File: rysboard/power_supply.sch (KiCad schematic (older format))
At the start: 34 parts, among them J19 Fan_Connector, Q4 DMP3036SSD-13, Q5 DMP3036SSD-13, U3 ST1S10, U6 L78L33_SO8

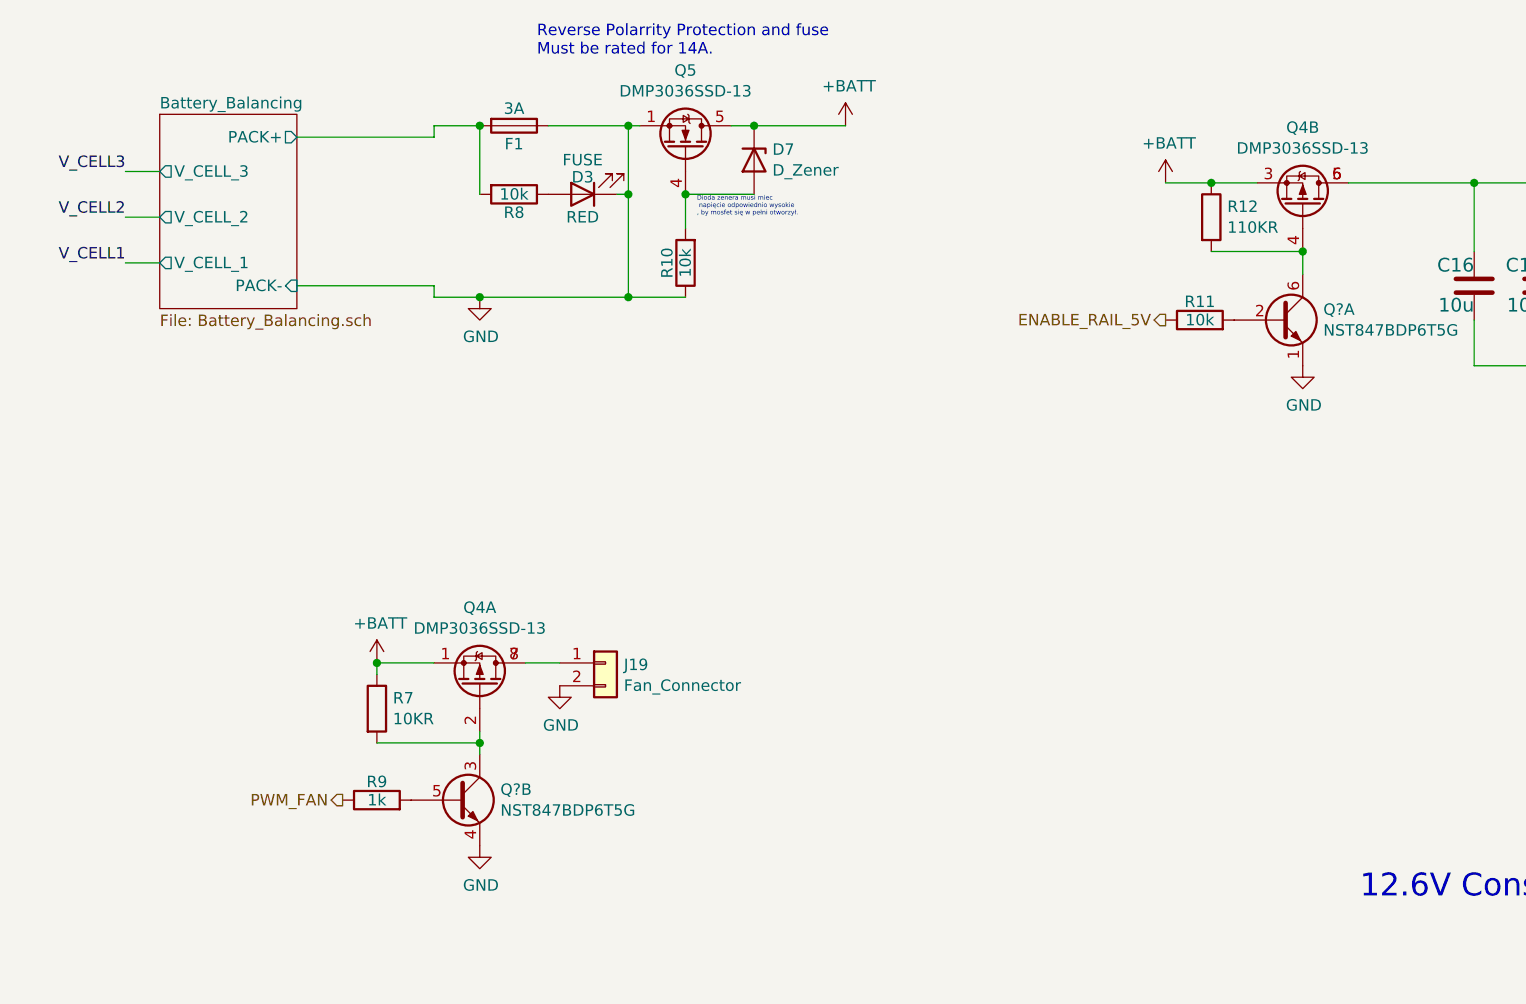
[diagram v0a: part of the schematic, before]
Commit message: added some of the analog sensors
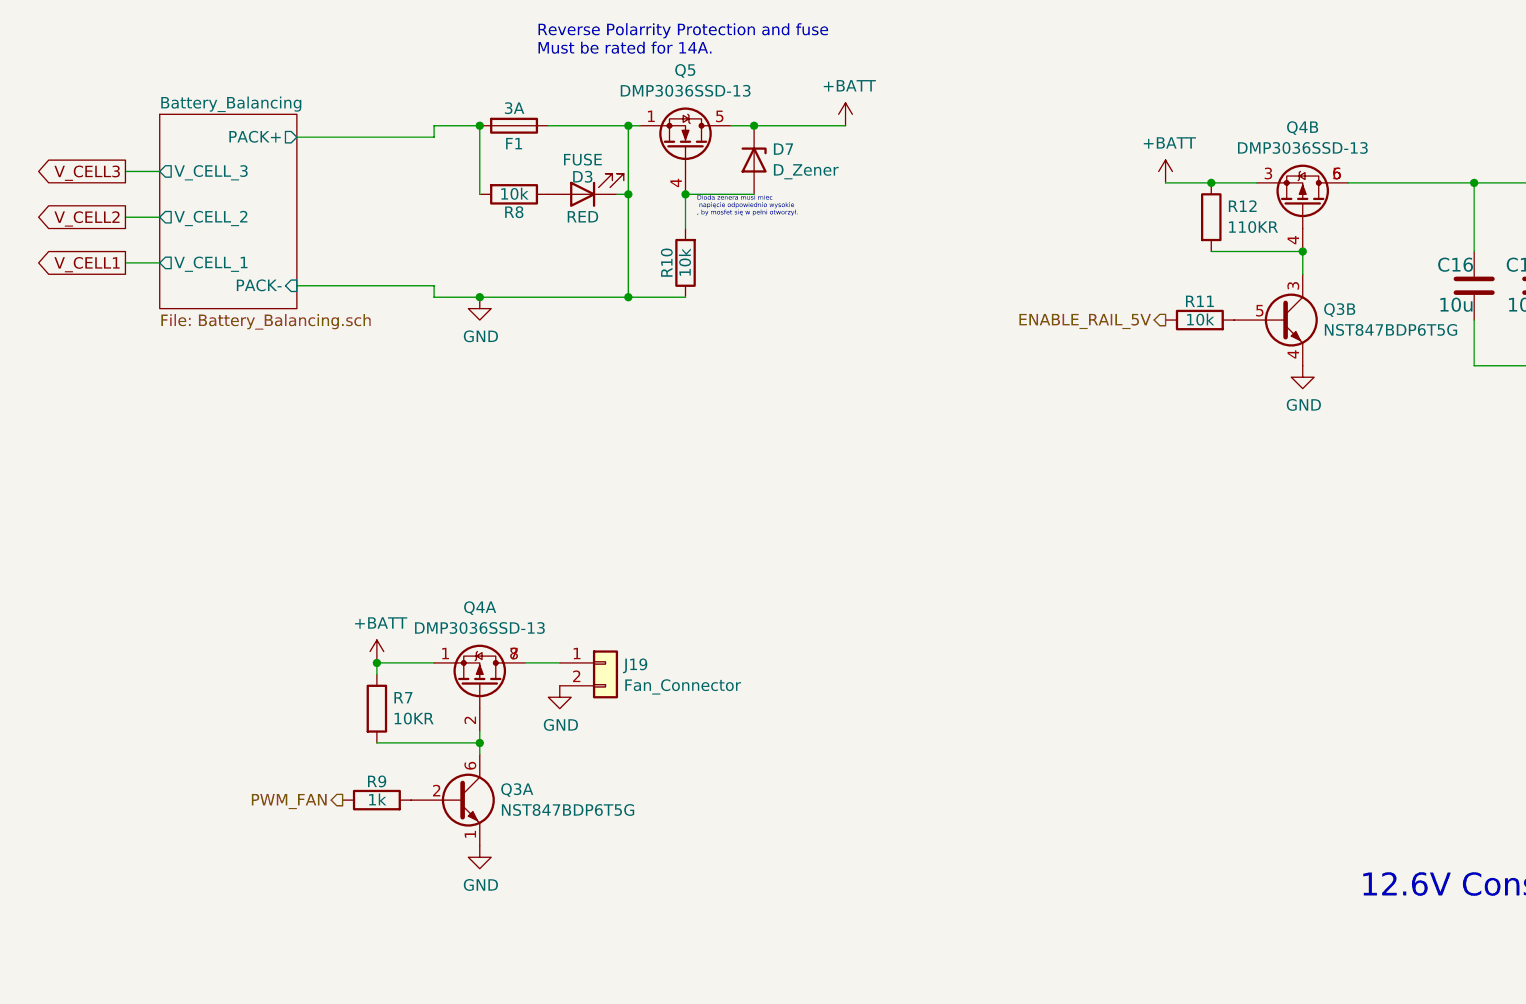
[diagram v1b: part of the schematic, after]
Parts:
- gave numbers to parts that had none: 1
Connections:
- net GND: now also Q3.1 (E1), Q3.4 (E2); no longer Q3.1 (E1), Q3.4 (E2)
- net at Q4.4 (G2), R12.2: now also Q3.3 (C2); no longer Q3.6 (C1)
- net at R11.2: now also Q3.5 (B2); no longer Q3.2 (B1)
- net at R9.2: now also Q3.2 (B1); no longer Q3.5 (B2)
- net at Q4.2 (G1), R7.2: now also Q3.6 (C1); no longer Q3.3 (C2)
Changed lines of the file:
@@
 Wire Wire Line
 	1000 1500 850  1500
-Text Label 850  1300 2    50   ~ 0
-V_CELL3
-Text Label 850  1500 2    50   ~ 0
-V_CELL2
-Text Label 850  1700 2    50   ~ 0
-V_CELL1
 $Sheet
 S 1000 1050 600  850
@@
 	7800 5300 7650 5300
 $Comp
-L rysboard:NST847BDP6T5G Q?
-U 1 1 606E7E9A
+L rysboard:NST847BDP6T5G Q3
+U 2 1 606E7E9A
 P 5900 1950
-F 0 "Q?" H 6090 1996 50  0000 L CNN
+F 0 "Q3" H 6090 1996 50  0000 L CNN
 F 1 "NST847BDP6T5G" H 6090 1905 50  0000 L CNN
 F 2 "Package_TO_SOT_SMD:SOT-963" H 6100 2050 50  0001 C CNN
 F 3 "~" H 5900 1950 50  0001 C CNN
-	1    5900 1950
-	1    0    0    -1
-$EndComp
-$Comp
-L rysboard:NST847BDP6T5G Q?
-U 2 1 606E8E92
+	2    5900 1950
+	1    0    0    -1
+$EndComp
+$Comp
+L rysboard:NST847BDP6T5G Q3
+U 1 1 606E8E92
 P 2300 4050
-F 0 "Q?" H 2490 4096 50  0000 L CNN
+F 0 "Q3" H 2490 4096 50  0000 L CNN
 F 1 "NST847BDP6T5G" H 2490 4005 50  0000 L CNN
 F 2 "Package_TO_SOT_SMD:SOT-963" H 2500 4150 50  0001 C CNN
 F 3 "~" H 2300 4050 50  0001 C CNN
-	2    2300 4050
-	1    0    0    -1
-$EndComp
+	1    2300 4050
+	1    0    0    -1
+$EndComp
+Text GLabel 850  1300 0    50   Output ~ 0
+V_CELL3
+Text GLabel 850  1500 0    50   Output ~ 0
+V_CELL2
+Text GLabel 850  1700 0    50   Output ~ 0
+V_CELL1
 $EndSCHEMATC

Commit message: Added eval board for STM32G031K8U6, rybsoard layout done, exact vals yet to be calculated
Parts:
- J19: symbol Connector_Generic:Conn_01x02 -> Connector_Generic:Conn_01x03
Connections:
- net GND: now also J19.3 (Pin_3); no longer J19.2 (Pin_2)
- net at Q4.7 (d), Q4.8 (d): now also J19.2 (Pin_2); no longer J19.1 (Pin_1)
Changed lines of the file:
@@
 Connection ~ 1950 3450
 $Comp
-L Connector_Generic:Conn_01x02 J19
+L Connector_Generic:Conn_01x03 J19
 U 1 1 606189C6
 P 2950 3450

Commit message: sensors enable added, Vref problem to solve
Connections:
- net GND: no longer F1.1, Q5.1 (S), Q5.2 (S), Q5.3 (S)
- new net: F1.1, Q5.1 (S), Q5.2 (S), Q5.3 (S)
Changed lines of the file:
@@
 $EndComp
-Wire Wire Line
-	3050 1100 2700 1100
-Connection ~ 3050 1100
 Wire Wire Line
 	2400 1100 2400 1400
 Wire Wire Line
 	3000 1400 3050 1400
-Wire Wire Line
-	3050 1400 3050 1100
 $Comp
 L power:GND #PWR018
@@
 	-1   0    0    1
 $EndComp
-Wire Wire Line
-	3100 1100 3050 1100
 $Comp
 L Device:R R8
@@
 Wire Wire Line
 	3050 1400 3050 1850
-Connection ~ 3050 1400
 Connection ~ 3050 1850
 Wire Wire Line
@@
 Text GLabel 850  1700 0    50   Output ~ 0
 V_CELL1
+Wire Wire Line
+	2700 1100 3100 1100
 $EndSCHEMATC

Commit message: new mosfet footprints
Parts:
- R12, R7: footprint (none) -> Resistor_SMD:R_0603_1608Metric
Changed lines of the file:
@@
 F 0 "R12" H 5670 1546 50  0000 L CNN
 F 1 "110KR" H 5670 1455 50  0000 L CNN
-F 2 "" V 5530 1500 50  0001 C CNN
+F 2 "Resistor_SMD:R_0603_1608Metric" V 5530 1500 50  0001 C CNN
 F 3 "~" H 5600 1500 50  0001 C CNN
 	1    5600 1500
@@
 F 0 "R7" H 2020 3696 50  0000 L CNN
 F 1 "10KR" H 2020 3605 50  0000 L CNN
-F 2 "" V 1880 3650 50  0001 C CNN
+F 2 "Resistor_SMD:R_0603_1608Metric" V 1880 3650 50  0001 C CNN
 F 3 "~" H 1950 3650 50  0001 C CNN
 	1    1950 3650

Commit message: Fixed library, added a few MOSFET layouts
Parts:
- removed D4, D5, D6: SK52, Diode_SMD:D_SMB, symbol Device:D_Schottky
- removed unit 1 of Q4
- removed Q5: DMP3036SSD-13, Package_SO:SO-8_5.3x6.2mm_P1.27mm, symbol Transistor_FET:Si7450DP
- added Q5: DMP3036SSD-13, Package_SO:SO-8_3.9x4.9mm_P1.27mm, symbol rysboard:DMP3036SSD-13
- added Q?: DMP2075UFDB, SamacSys_Parts:DMP2075UFDB7, symbol rysboard:DMP2075UFDB
- Q4: footprint Package_SO:SO-8_5.3x6.2mm_P1.27mm -> Package_SO:SO-8_3.9x4.9mm_P1.27mm
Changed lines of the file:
@@
 F 1 "1uF" H 2550 6950 60  0000 R TNN
 F 2 "Capacitor_SMD:C_0603_1608Metric" H 2450 7090 60  0001 C CNN
-F 3 "" H 2450 7090 60  0001 C CNN
+F 3 "~" H 2450 7090 60  0001 C CNN
 	1    2550 7000
 	1    0    0    -1
@@
 F 1 "100n" H 3750 6950 60  0000 R TNN
 F 2 "Capacitor_SMD:C_0603_1608Metric" H 3650 7090 60  0001 C CNN
-F 3 "" H 3650 7090 60  0001 C CNN
+F 3 "~" H 3650 7090 60  0001 C CNN
 	1    3750 7000
 	1    0    0    -1
@@
 F 1 "10u" H 9875 1750 60  0000 R TNN
 F 2 "Capacitor_SMD:C_1206_3216Metric" H 9775 1890 60  0001 C CNN
-F 3 "" H 9775 1890 60  0000 C CNN
+F 3 "~" H 9775 1890 60  0000 C CNN
 	1    9875 1800
 	1    0    0    -1
@@
 F 1 "10u" H 10175 1750 60  0000 R TNN
 F 2 "Capacitor_SMD:C_1206_3216Metric" H 10075 1890 60  0001 C CNN
-F 3 "" H 10075 1890 60  0000 C CNN
+F 3 "~" H 10075 1890 60  0000 C CNN
 	1    10175 1800
 	1    0    0    -1
@@
 F 1 "100n" H 10475 1750 60  0000 R TNN
 F 2 "Capacitor_SMD:C_0603_1608Metric" H 10375 1890 60  0001 C CNN
-F 3 "" H 10375 1890 60  0001 C CNN
+F 3 "~" H 10375 1890 60  0001 C CNN
 	1    10475 1800
 	1    0    0    -1
@@
 F 1 "3.3uH" V 9125 1350 50  0000 C CNN
 F 2 "rysboard:L_6.7x6.7_H2.2" H 9025 1350 50  0001 C CNN
-F 3 "https://www.tme.eu/pl/details/hpi0624-3r3/dlawiki-smd-mocy/ferrocore/" H 9025 1350 50  0001 C CNN
+F 3 "~" H 9025 1350 50  0001 C CNN
 F 4 "HPI0624-3R3" V 8975 1325 50  0000 C CNN "Model"
 	1    9025 1350
@@
 F 1 "100n" H 7350 1750 60  0000 R TNN
 F 2 "Capacitor_SMD:C_0603_1608Metric" H 7250 1890 60  0001 C CNN
-F 3 "" H 7250 1890 60  0001 C CNN
+F 3 "~" H 7250 1890 60  0001 C CNN
 	1    7350 1800
 	1    0    0    -1
@@
 F 1 "10u" H 7050 1750 60  0000 R TNN
 F 2 "Capacitor_SMD:C_1206_3216Metric" H 6950 1890 60  0001 C CNN
-F 3 "" H 6950 1890 60  0000 C CNN
+F 3 "~" H 6950 1890 60  0000 C CNN
 	1    7050 1800
 	1    0    0    -1
@@
 F 1 "10u" H 6750 1750 60  0000 R TNN
 F 2 "Capacitor_SMD:C_1206_3216Metric" H 6650 1890 60  0001 C CNN
-F 3 "" H 6650 1890 60  0000 C CNN
+F 3 "~" H 6650 1890 60  0000 C CNN
 	1    6750 1800
 	1    0    0    -1
@@
 $EndComp
 $Comp
-L Device:D_Schottky D5
-U 1 1 5EC1A2D5
-P 2250 6550
-F 0 "D5" H 2250 6650 50  0000 C CNN
-F 1 "SK52" H 2250 6450 50  0000 C CNN
-F 2 "Diode_SMD:D_SMB" H 2250 6550 50  0001 C CNN
-F 3 "~" H 2250 6550 50  0001 C CNN
-	1    2250 6550
-	-1   0    0    1
-$EndComp
-$Comp
 L Device:R R8
 U 1 1 5EC1A2DB
@@
 Connection ~ 2550 6850
 $Comp
-L Transistor_FET:Si7450DP Q5
-U 1 1 5FEC0C71
-P 3300 1200
-F 0 "Q5" V 3642 1200 50  0000 C CNN
-F 1 "DMP3036SSD-13" V 3551 1200 50  0000 C CNN
-F 2 "Package_SO:SO-8_5.3x6.2mm_P1.27mm" H 3500 1125 50  0001 L CIN
-F 3 "http://www.vishay.com/docs/70209/70209.pdf" H 3300 1200 50  0001 L CNN
-	1    3300 1200
-	0    1    -1   0
-$EndComp
-$Comp
 L Device:R R10
 U 1 1 5FECF6D8
@@
 Wire Wire Line
 	3600 1400 3300 1400
-Connection ~ 3300 1400
 Wire Wire Line
 	4000 1100 3600 1100
@@
 Text Notes 2650 800  0    50   ~ 0
 Reverse Polarrity Protection and fuse\nMust be rated for 14A.\n
-$Comp
-L Device:D_Schottky D4
-U 1 1 5FE2C885
-P 2250 6250
-F 0 "D4" H 2250 6350 50  0000 C CNN
-F 1 "SK52" H 2250 6150 50  0000 C CNN
-F 2 "Diode_SMD:D_SMB" H 2250 6250 50  0001 C CNN
-F 3 "~" H 2250 6250 50  0001 C CNN
-	1    2250 6250
-	-1   0    0    1
-$EndComp
 Wire Wire Line
 	2400 6550 2550 6550
@@
 	1    0    0    -1
 $EndComp
-$Comp
-L rysboard:DMP3036SSD-13 Q4
-U 2 1 605CD694
-P 6000 1450
-F 0 "Q4" V 6342 1450 50  0000 C CNN
-F 1 "DMP3036SSD-13" V 6251 1450 50  0000 C CNN
-F 2 "Package_SO:SO-8_5.3x6.2mm_P1.27mm" H 6200 1375 50  0001 L CIN
-F 3 "http://www.vishay.com/docs/70209/70209.pdf" H 6000 1450 50  0001 L CNN
-	2    6000 1450
-	0    1    -1   0
-$EndComp
 Wire Wire Line
 	6200 1350 6750 1350
@@
 	5600 1350 5400 1350
 Connection ~ 5600 1350
-Wire Wire Line
-	6000 1650 5600 1650
 $Comp
 L Device:R R11
@@
 Wire Wire Line
 	6000 1650 6000 1750
-Connection ~ 6000 1650
 $Comp
 L power:GND #PWR036
@@
 	1    0    0    -1
 $EndComp
-$Comp
-L rysboard:DMP3036SSD-13 Q4
-U 1 1 60603F20
-P 2400 3550
-F 0 "Q4" V 2742 3550 50  0000 C CNN
-F 1 "DMP3036SSD-13" V 2651 3550 50  0000 C CNN
-F 2 "Package_SO:SO-8_5.3x6.2mm_P1.27mm" H 2600 3475 50  0001 L CIN
-F 3 "http://www.vishay.com/docs/70209/70209.pdf" H 2400 3550 50  0001 L CNN
-	1    2400 3550
-	0    1    -1   0
-$EndComp
 Wire Wire Line
 	2400 3750 2400 3800
@@
 Wire Wire Line
 	1950 6250 2100 6250
-$Comp
-L Device:D_Schottky D6
-U 1 1 6066D30E
-P 2250 6850
-F 0 "D6" H 2250 6950 50  0000 C CNN
-F 1 "SK52" H 2250 6750 50  0000 C CNN
-F 2 "Diode_SMD:D_SMB" H 2250 6850 50  0001 C CNN
-F 3 "~" H 2250 6850 50  0001 C CNN
-	1    2250 6850
-	-1   0    0    1
-$EndComp
 Wire Wire Line
 	2550 6550 2550 6250
@@
 Wire Wire Line
 	2700 1100 3100 1100
+Wire Wire Line
+	5600 1650 6000 1650
+$Comp
+L rysboard:DMP3036SSD-13 Q4
+U 2 1 6051D51B
+P 3300 1200
+F 0 "Q4" V 3642 1200 50  0000 C CNN
+F 1 "DMP3036SSD-13" V 3551 1200 50  0000 C CNN
+F 2 "Package_SO:SO-8_3.9x4.9mm_P1.27mm" H 3500 1125 50  0001 L CIN
+F 3 "" H 3300 1200 50  0001 L CNN
+	2    3300 1200
+	0    -1   -1   0
+$EndComp
+Connection ~ 3300 1400
+$Comp
+L rysboard:DMP3036SSD-13 Q5
+U 1 1 6051EA37
+P 6000 1450
+F 0 "Q5" V 6342 1450 50  0000 C CNN
+F 1 "DMP3036SSD-13" V 6251 1450 50  0000 C CNN
+F 2 "Package_SO:SO-8_3.9x4.9mm_P1.27mm" H 6200 1375 50  0001 L CIN
+F 3 "" H 6000 1450 50  0001 L CNN
+	1    6000 1450
+	0    1    -1   0
+$EndComp
+$Comp
+L rysboard:DMP2075UFDB Q?
+U 1 1 605E5DAF
+P 2400 3550
+F 0 "Q?" V 2742 3550 50  0000 C CNN
+F 1 "DMP2075UFDB" V 2651 3550 50  0000 C CNN
+F 2 "SamacSys_Parts:DMP2075UFDB7" H 2600 3475 50  0001 L CIN
+F 3 "" H 2400 3550 50  0001 L CNN
+	1    2400 3550
+	0    1    -1   0
+$EndComp
 $EndSCHEMATC

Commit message: battery Balancing specified
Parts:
- removed Q?: DMP2075UFDB, SamacSys_Parts:DMP2075UFDB7, symbol rysboard:DMP2075UFDB
- added Q?: DMP3036SSD-13, Package_SO:SO-8_3.9x4.9mm_P1.27mm, symbol rysboard:DMP3036SSD-13
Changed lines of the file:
@@
 $EndComp
 $Comp
-L rysboard:DMP2075UFDB Q?
-U 1 1 605E5DAF
+L rysboard:DMP3036SSD-13 Q?
+U 1 1 605FF267
 P 2400 3550
 F 0 "Q?" V 2742 3550 50  0000 C CNN
-F 1 "DMP2075UFDB" V 2651 3550 50  0000 C CNN
-F 2 "SamacSys_Parts:DMP2075UFDB7" H 2600 3475 50  0001 L CIN
+F 1 "DMP3036SSD-13" V 2651 3550 50  0000 C CNN
+F 2 "Package_SO:SO-8_3.9x4.9mm_P1.27mm" H 2600 3475 50  0001 L CIN
 F 3 "" H 2400 3550 50  0001 L CNN
 	1    2400 3550
